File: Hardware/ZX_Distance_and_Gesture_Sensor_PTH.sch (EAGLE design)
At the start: 50 parts, among them Q1 MMBT2222A, Q2 MOSFET-NCHANNEL2N7002PW, U1 BRM-2508VERT

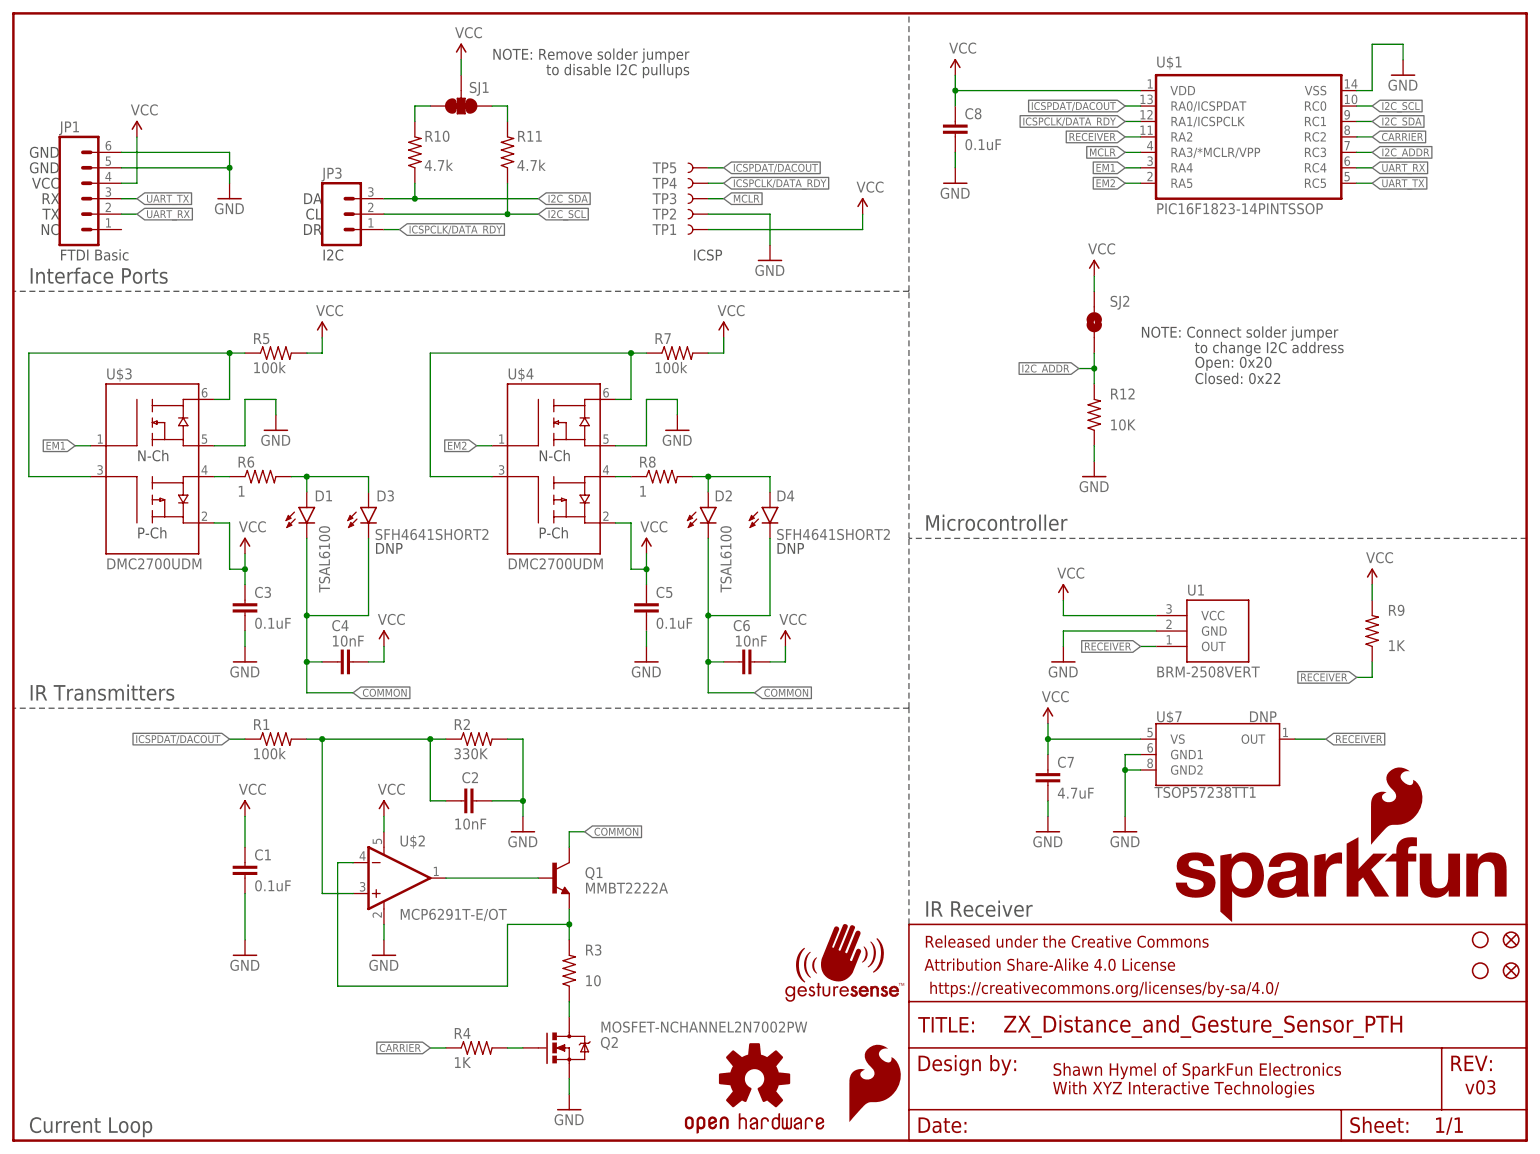
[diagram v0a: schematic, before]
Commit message: Updated REFDES numbers. Changed to v04.
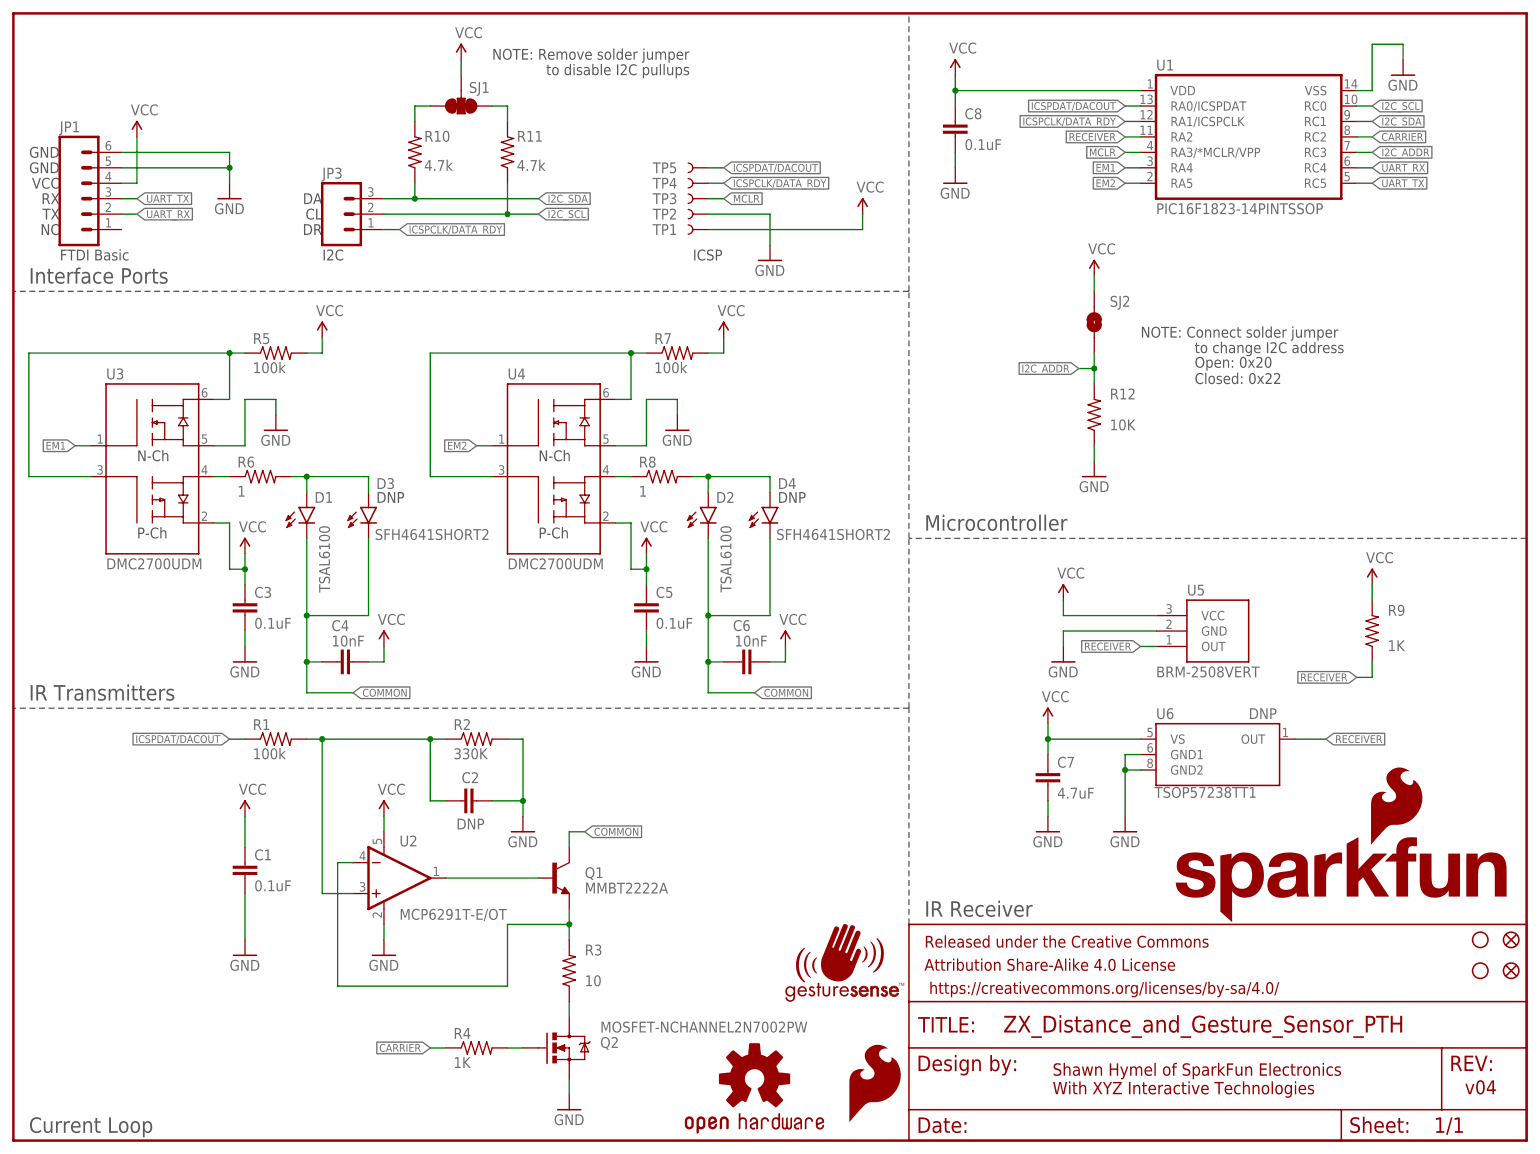
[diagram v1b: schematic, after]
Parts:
- removed U$1: PIC16F1823-14PINTSSOP, SparkFun-DigitalIC:PIC16F1823-14PINTSSOP
- added U5: BRM-2508VERT, SparkFun-Sensors:BRM-2508VERT
- C2: value 10nF -> DNP; device SparkFun-Capacitors:10NF/10000PF-50V-10%(0603) -> SparkFun-Capacitors:CAP0603-CAP
- U1: value BRM-2508VERT -> PIC16F1823-14PINTSSOP; device SparkFun-Sensors:BRM-2508VERT -> SparkFun-DigitalIC:PIC16F1823-14PINTSSOP
- renumbered U$2 to U2, U$3 to U3, U$4 to U4, U$7 to U6
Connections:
- net CARRIER: now also U1.RC2; no longer U$1.RC2
- net EM1: now also U1.RA4; no longer U$1.RA4
- net EM2: now also U1.RA5; no longer U$1.RA5
- net GND: now also U1.VSS, U5.GND; no longer U$1.VSS, U1.GND
- net I2C_ADDR: now also U1.RC3; no longer U$1.RC3
- net I2C_SCL: now also U1.RC0; no longer U$1.RC0
- net I2C_SDA: now also U1.RC1; no longer U$1.RC1
- net ICSPCLK/DATA_RDY: now also U1.RA1/ICSPCLK; no longer U$1.RA1/ICSPCLK
- net ICSPDAT/DACOUT: now also U1.RA0/ICSPDAT; no longer U$1.RA0/ICSPDAT
- net MCLR: now also U1.RA3/*MCLR/VPP; no longer U$1.RA3/*MCLR/VPP
- net RECEIVER: now also U1.RA2, U5.OUT; no longer U$1.RA2, U1.OUT
- net UART_RX: now also U1.RC4; no longer U$1.RC4
- net UART_TX: now also U1.RC5; no longer U$1.RC5
- net VCC: now also U1.VDD, U5.VCC; no longer U$1.VDD, U1.VCC
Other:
- note added: "v04"
- note removed: "v03"
